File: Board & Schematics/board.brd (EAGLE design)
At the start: 10.2 x 14.2 mm, 18 parts, among them U1 ATTINY-85

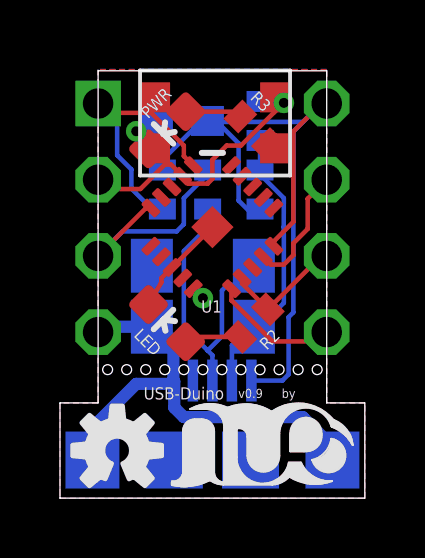
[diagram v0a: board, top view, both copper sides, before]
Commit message: added reset switch to support bootloader
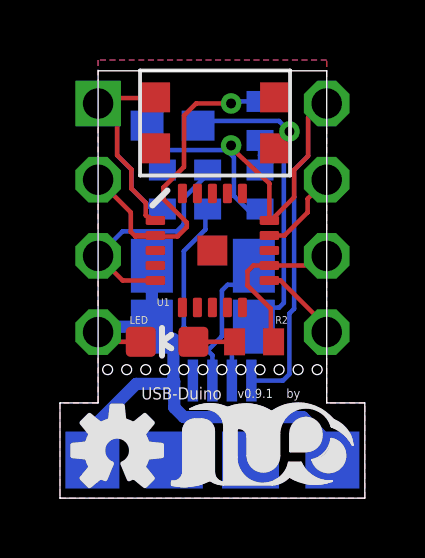
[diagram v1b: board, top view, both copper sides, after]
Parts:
- removed PWR: (no value), SparkFun-LED:LED-0603
- removed R3: 10k, rcl:R0402
- moved U1 0.78 mm to (3.81, 3.81), turned to 0 degrees
- moved LED 0.62 mm to (2.30, 0.77), turned to 90 degrees
- moved R2 0.62 mm to (5.20, 0.77), turned to 0 degrees
- moved C1 0.35 mm to (2.48, 7.97), turned to 180 degrees
- renumbered U$3 to RESET
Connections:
- removed net N$1: JP1.1, R1.2, U1.1
- removed net N$2: PWR.A, R3.1
- new net N$3: JP1.1, R1.2, RESET.1, U1.1
- net +5V: no longer R3.2
- net GND: now also RESET.4; no longer PWR.C
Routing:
- net N$3: track 0.00 -> 11.3 mm
- net N$1: track 8.85 -> 0.00 mm
- net D-: track 9.23 -> 12.0 mm
- net +5V: track 28.9 -> 26.5 mm, vias 0 -> 1
- net N$2: track 2.02 -> 0.00 mm
- net GND: track 22.2 -> 23.8 mm, vias 2 -> 1
- net N$4: track 4.26 -> 2.73 mm
- net N$26: track 4.07 -> 5.56 mm
- net N$8: track 9.43 -> 10.8 mm
- net N$25: track 4.26 -> 2.95 mm
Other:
- board text added: "v0.9.1"
- board text removed: "v0.9"
